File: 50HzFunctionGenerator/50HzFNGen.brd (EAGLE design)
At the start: 99 x 77.1 mm, 23 parts, among them IC2 7812L, IC4 TL082P, X2 MAB32

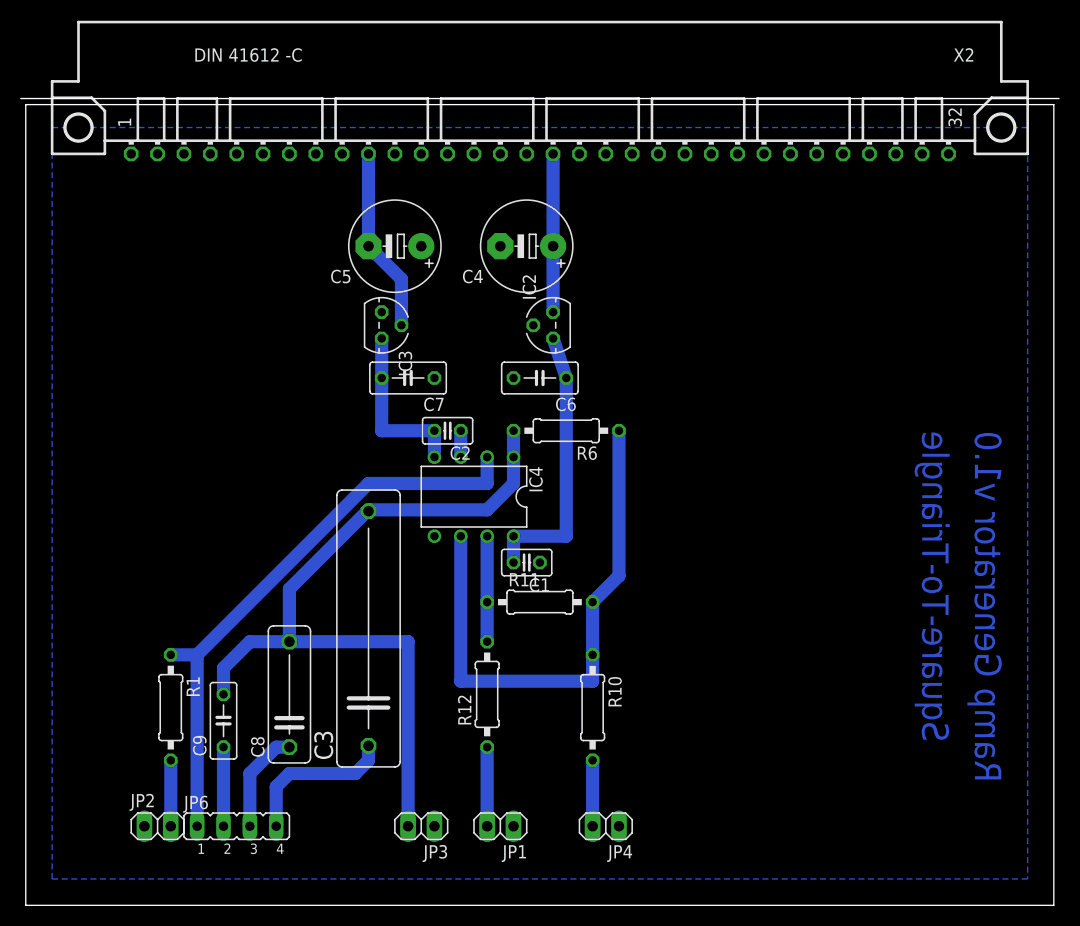
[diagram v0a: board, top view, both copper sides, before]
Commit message: Some changes to make the function generator board work
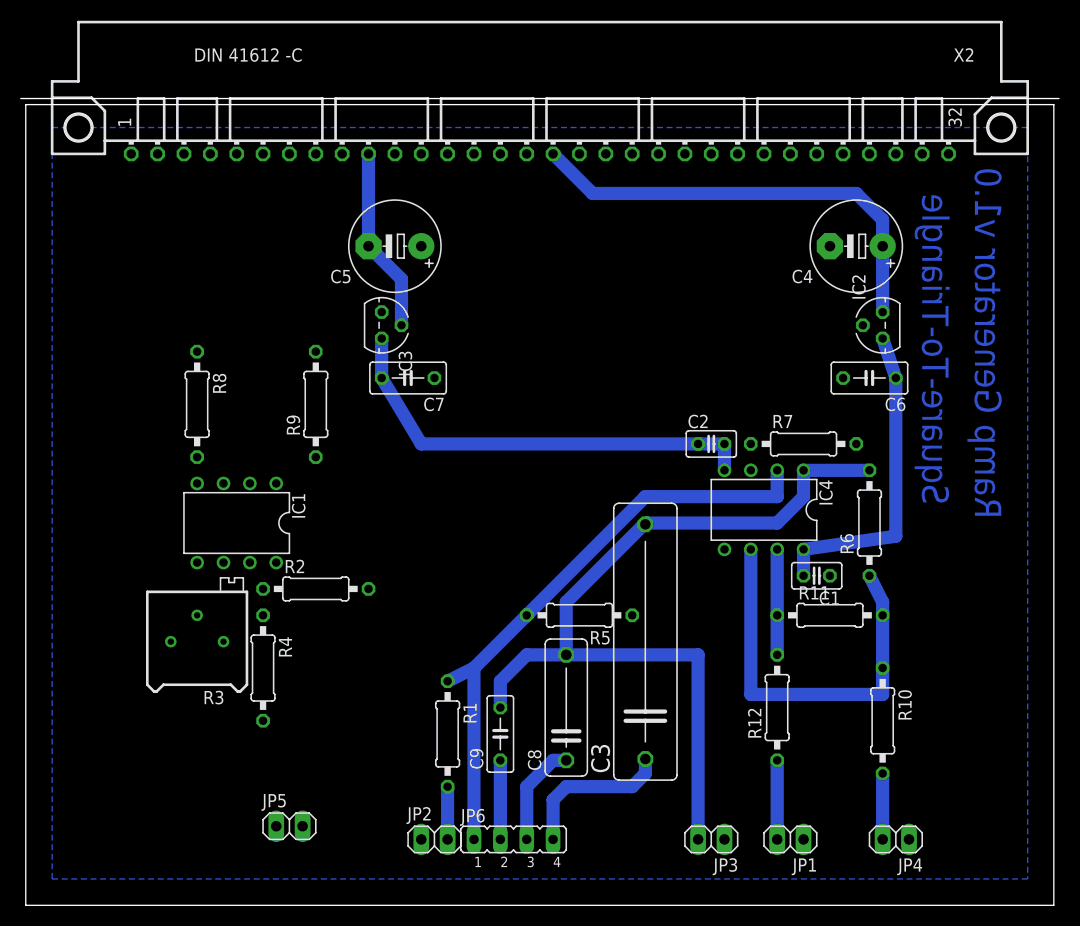
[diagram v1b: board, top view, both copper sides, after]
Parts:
- added IC1: LM311N, linear:DIL08
- added JP5: 5V Hz Square wave in, pinhead:1X02
- added R2, R4, R8, R9: 20k, resistor:0207/10
- added R3: (no value), resistor:RTRIM64P
- added R5, R7: 100k, resistor:0207/10
- moved C4 31.8 mm to (80.0, 63.5)
- moved C6 31.8 mm to (81.3, 50.8)
- moved IC2 31.8 mm to (82.5, 55.9)
- moved R6 30.5 mm to (81.3, 36.8), turned to 90 degrees
- moved C1 28.0 mm to (76.2, 31.8)
- moved IC4 28.0 mm to (71.1, 38.1)
- moved JP3 28.0 mm to (66.0, 6.35)
- moved JP1 28.0 mm to (73.7, 6.35)
- moved R10 28.0 mm to (82.5, 17.8)
- moved R11 28.0 mm to (77.5, 27.9)
- moved R12 28.0 mm to (72.4, 19.1)
- moved JP4 28.0 mm to (83.8, 6.35)
- moved R1 26.8 mm to (40.6, 16.5)
- moved C8 26.7 mm to (52.1, 19.1)
- moved JP6 26.7 mm to (47.0, 6.35)
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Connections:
- new net N$12: IC1.7, JP2.1, R2.1
- new net N$16: IC1.5, R3.3
- new net N$18: IC1.6, R3.1
- new net N$19: R3.2, R4.1
- new net N$20: IC4.3, R7.1
- new net N$23: IC1.2, JP5.2
- new net N$25: IC1.3, R8.1, R9.2
- net +12V: now also IC1.8, R2.2, R4.2, R9.1
- net -12V: now also IC1.1, IC1.4, R8.2
- net GND: now also JP5.1, R7.2; no longer IC4.3, JP2.1
- net N$14: now also R5.1
- net N$17: now also R5.2
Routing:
- net +15V: track 15.2 -> 43.3 mm
- net -12V: track 16.5 -> 43.0 mm
- net N$7: track 51.9 -> 38.4 mm
- net N$14: track 75.1 -> 81.5 mm
- net +12V: track 26.9 -> 30.8 mm
- net GND: track 2.54 -> 0.00 mm
- net N$17: track 56.4 -> 57.9 mm
- net N$13: track 6.35 -> 5.08 mm

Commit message: finished version of the board
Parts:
- removed JP5: 5V Hz Square wave in, pinhead:1X02
- added JP7: (no value), jumper:JP2
- moved R8 48.3 mm to (64.8, 47.0), turned to 180 degrees
- moved R9 44.9 mm to (72.4, 41.9)
- moved R3 44.6 mm to (61.0, 21.6)
- moved R4 43.5 mm to (66.0, 27.9), turned to 0 degrees
- moved IC1 43.2 mm to (63.5, 38.1)
- moved R2 41.9 mm to (69.8, 31.8)
- moved R6 36.4 mm to (45.7, 44.5), turned to 180 degrees
- moved C6 35.8 mm to (45.7, 54.6), turned to 90 degrees
- moved C2 31.8 mm to (34.3, 44.5)
- moved C4 31.8 mm to (48.3, 63.5)
- moved IC4 31.8 mm to (39.4, 38.1)
- moved JP3 31.8 mm to (34.3, 6.35)
- moved C1 31.8 mm to (44.5, 31.8)
- moved IC2 31.8 mm to (50.8, 55.9)
- moved JP1 31.8 mm to (41.9, 6.35)
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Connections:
- net GND: now also JP7.3, X2.A11, X2.A12, X2.A14, X2.A15, X2.A16; no longer JP5.1
- net N$12: now also JP7.2; no longer JP2.1
- net N$23: now also JP7.1; no longer JP5.2
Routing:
- net N$23: track 0.00 -> 51.8 mm
- net +12V: track 30.8 -> 79.0 mm
- net N$12: track 0.00 -> 28.2 mm
- net +15V: track 43.3 -> 15.2 mm
- net -12V: track 43.0 -> 61.3 mm, vias 0 -> 6
- net N$25: track 0.00 -> 13.8 mm
- net N$16: track 0.00 -> 13.2 mm
- net N$18: track 0.00 -> 13.0 mm
- net N$7: track 38.4 -> 50.8 mm
- net N$14: track 81.5 -> 73.4 mm
- net N$20: track 0.00 -> 6.13 mm
- net N$19: track 0.00 -> 3.81 mm
- net N$4: track 15.1 -> 11.3 mm
- net N$11: track 9.94 -> 8.15 mm
- net GND: track 0.00 -> 0.64 mm
